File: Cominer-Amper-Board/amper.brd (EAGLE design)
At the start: 54.3 x 61 mm, 3 parts, among them U1 ESP-07

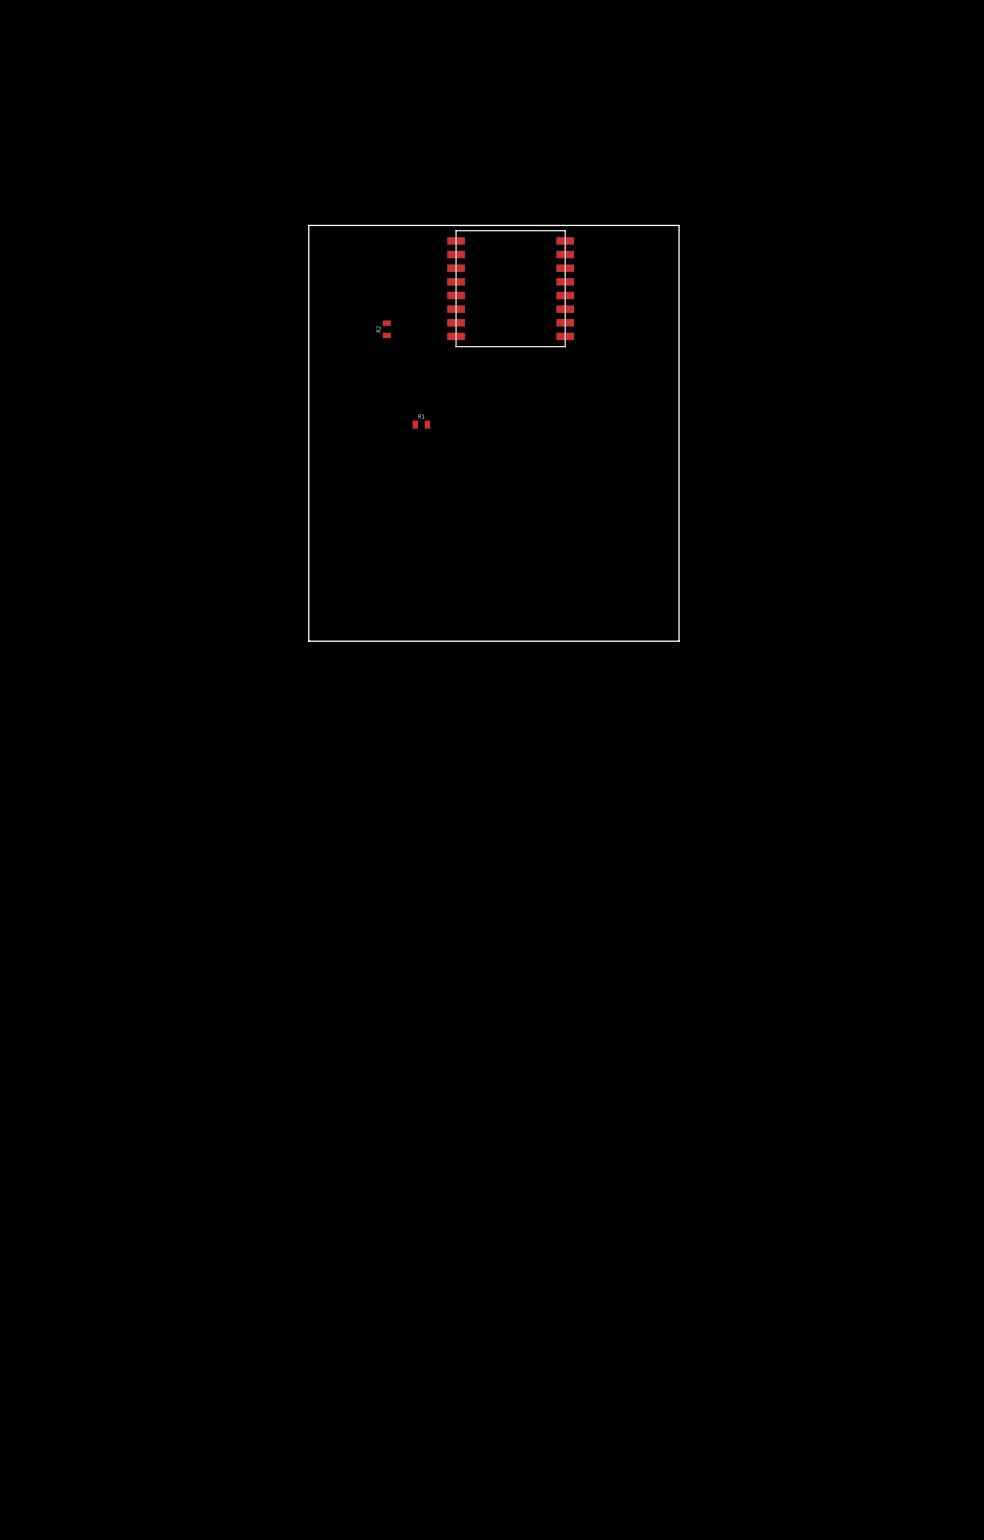
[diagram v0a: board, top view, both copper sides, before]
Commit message: add usb to serialport circuit and lm1117 regulator
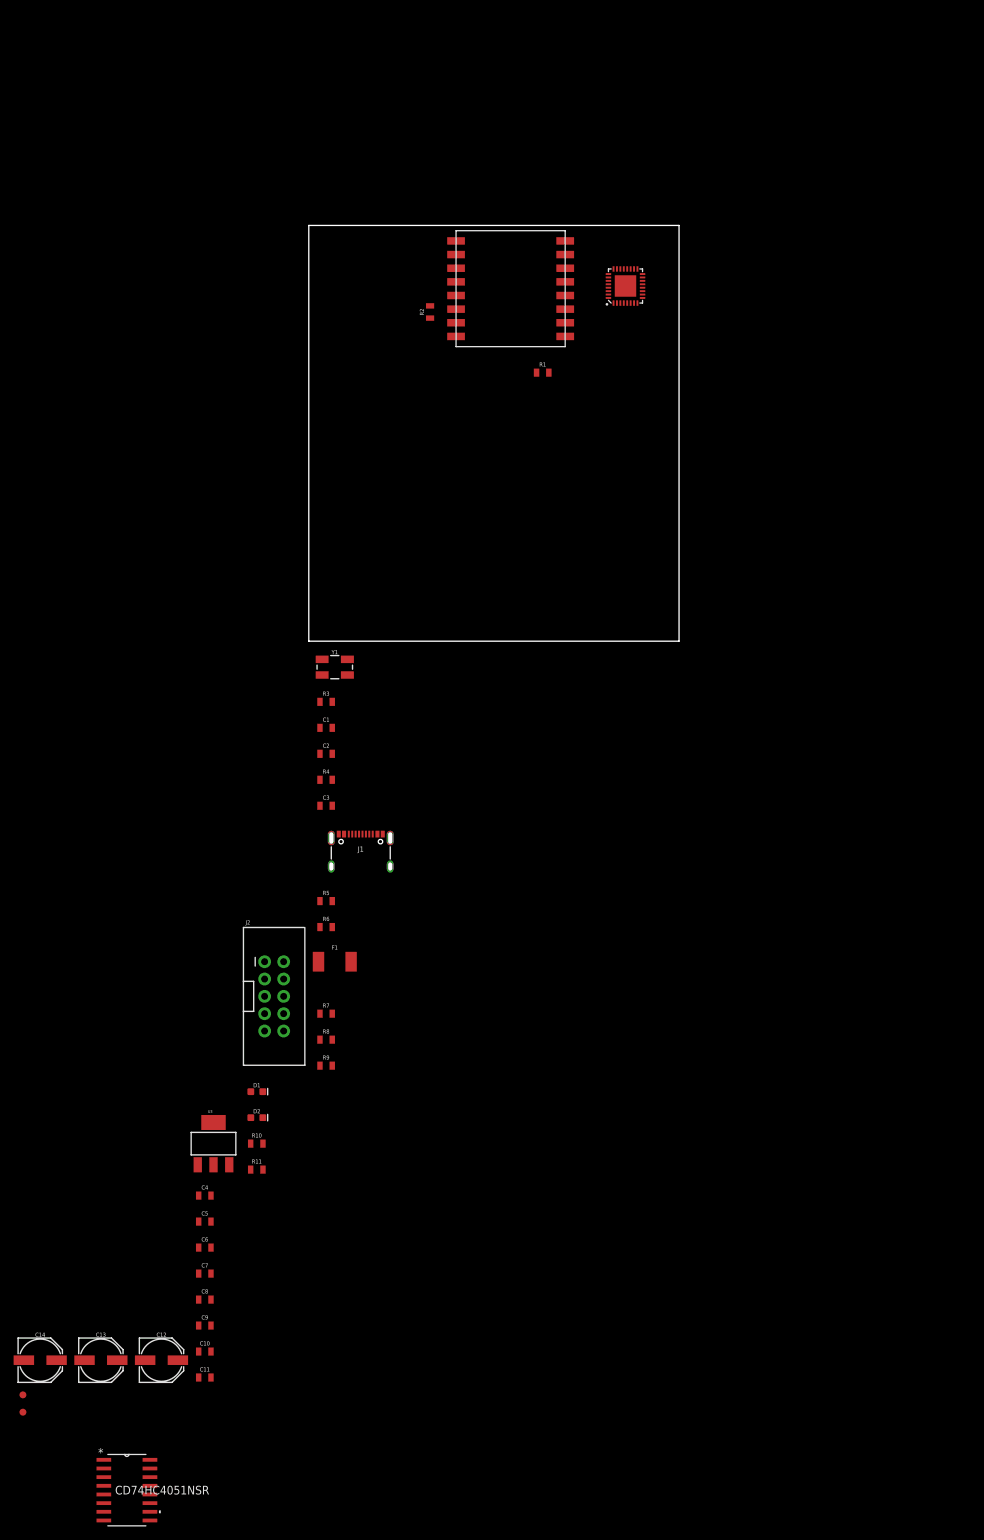
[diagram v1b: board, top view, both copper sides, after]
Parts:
- added C1, C2, C5, C6, C7, C8: 22p, SparkFun-Capacitors:0805
- added C10, C11, C3, C4, C9: 1u, SparkFun-Capacitors:0805
- added C12, C13, C14: 100uF, SparkFun-Capacitors:PANASONIC_D
- added D1, D2: Yellow, SparkFun-LED:LED-0603
- added F1: 500mA, SparkFun-Fuses:1812
- added J1: (no value), SparkFun-Connectors:USB-C-16P-2LAYER-PADS
- added J2: AVR_SPI_PROG_5X2LOCK, SparkFun-Connectors:2X5-SHROUDED_LOCK
- added R10, R11: 1k, SparkFun-Resistors:0805
- added R3: 10M, SparkFun-Resistors:0805
- added R4, R7, R8, R9: 10k, SparkFun-Resistors:0805
- added R5, R6: 22, SparkFun-Resistors:0805
- added TP2: 3.3v, SparkFun-Connectors:PAD.03X.04
- added TP3: 5v, SparkFun-Connectors:PAD.03X.04
- added U2: ATMEGA16U2, Cominer-Microcontroller:QFN32
- added U3: LM1117-3.3v, SparkFun-IC-Power:SOT223
- added U4: CD74HC4051NSR, Cominer-CD74HC4051NSR:NS16
- added Y1: 16MHz, SparkFun-Clocks:CRYSTAL-SMD-5X3.2-4PAD
- R1, R2: value (none) -> 10k
- moved R1 19.3 mm to (34.3, 39.4)
- moved R2 6.84 mm to (17.8, 48.3)
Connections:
- net ADC renamed ADC_ESP
- net RST renamed RST_ESP
- removed net RX: U1.RX0
- removed net TX: U1.TX0
- new net 5V: C10.2, C11.2, C12.+, C13.+, C14.+, C9.2, F1.2, J2.2, R10.2, R11.2, R4.1, R9.2, TP3.P$1, U2.31, U2.32, U2.4, U3.3
- new net MISO_AVR: J2.9, U2.17
- new net MOSI_AVR: J2.1, U2.16
- new net N$1: C1.2, R3.1, U2.1, Y1.3
- new net N$10: F1.1, J1.VBUS1, J1.VBUS2
- new net N$11: R7.1, U2.8
- new net N$12: D1.C, U2.11
- new net N$13: D2.A, R10.1
- new net N$15: D1.A, R11.1
- new net N$2: C2.2, R3.2, U2.2, Y1.1
- new net N$3: C3.2, U2.27
- new net N$4: D2.C, U2.10
- new net N$5: R8.1, U2.9
- new net N$6: R6.2, U2.30
- new net N$7: R5.2, R9.1, U2.29
- new net N$8: J1.A6, J1.B6, R5.1
- new net N$9: J1.A7, J1.B7, R6.1
- new net RST_AVR: J2.5, R4.2, U2.24
- new net RX_ESP: R8.2, U1.RX0
- new net SCK_AVR: J2.7, U2.15
- new net TX_ESP: R7.2, U1.TX0
- new net VCC: U4.16
- new net VEE: U4.7
- net 3.3V: now also C4.2, C5.2, C6.2, C7.2, C8.2, TP2.P$1, U3.2
- net GND: now also C1.1, C10.1, C11.1, C12.-, C13.-, C14.-, C2.1, C3.1, C4.1, C5.1, C6.1, C7.1, C8.1, C9.1, J1.GND, J1.GND2, J1.SHLD1, J1.SHLD2, J1.SHLD3, J1.SHLD4, J2.10, J2.4, J2.6, J2.8, U2.28, U2.3, U2.EP, U3.1, U4.8

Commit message: all devices were order
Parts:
- removed C10, C11, C9: 1u, SparkFun-Capacitors:0805
- removed C13, C14: 100uF, SparkFun-Capacitors:PANASONIC_D
- removed C7, C8: 22p, SparkFun-Capacitors:0805
- removed D1, D2: Yellow, SparkFun-LED:LED-0603
- removed R10, R11: 1k, SparkFun-Resistors:0805
- removed R7, R8: 10k, SparkFun-Resistors:0805
- removed TP2: 3.3v, SparkFun-Connectors:PAD.03X.04
- removed TP3: 5v, SparkFun-Connectors:PAD.03X.04
- added C17, C18, C19: 0.1u, SparkFun-Capacitors:0805
- added C20: 1u, SparkFun-Capacitors:0805
- added C23: 100uF, SparkFun-Capacitors:PANASONIC_D
- added D3: STATUS, SparkFun-LED:LED-0603
- added D4: ALARM, SparkFun-LED:LED-0603
- added D5: POWER, SparkFun-LED:LED-0603
- added IC1: OP-AMP, SparkFun-IC-Amplifiers:SO08
- added J3, J4, J5, J6: AUDIO_JACK_3.5MM_PTH, SparkFun-Connectors:AUDIO-JACK
- added J7: MOLEX-CPU-POWER, Cominer-Connectors:MOLEX-5.08-4PIN
- added J8: POWER_JACKSLT, SparkFun-Connectors:POWER_JACK_SLOT
- added Q1, Q2, Q3, Q4, Q5, Q6: 220mA/50V/3.5Ω, SparkFun-DiscreteSemi:SOT23-3
- added Q7: 20V/2A, SparkFun-DiscreteSemi:SOT23-3
- added R12, R13, R14, R15, R16, R17, R18, R19, R20, R21, R22, R23, R24, R25: 10k, SparkFun-Resistors:0805
- added R26, R27, R28: 1k, SparkFun-Resistors:0805
- added U5, U6: ADS1015, SparkFun-IC-Conversion:MSOP10
- C4: value 1u -> 0.1u
- C5, C6: value 22p -> 0.1u
- U4: value CD74HC4051NSR -> LM1117-5v; device Cominer-CD74HC4051NSR:NS16 -> SparkFun-IC-Power:SOT223
- moved U4 198.2 mm to (45.8, 60.0), turned to 180 degrees
- moved C12 189.3 mm to (45.7, 71.5), turned to 90 degrees
- moved C6 159.8 mm to (36.8, 62.2), turned to 270 degrees
- moved R9 155.4 mm to (66.2, 79.5), turned to 90 degrees
- moved C4 153.3 mm to (68.9, 46.8), turned to 90 degrees
- moved C5 152.2 mm to (68.9, 41.7), turned to 90 degrees
- moved J2 148.0 mm to (84.0, 66.1)
- moved F1 144.9 mm to (74.6, 79.4)
- moved U3 141.2 mm to (31.4, 60.0), turned to 180 degrees
- moved R6 138.8 mm to (69.9, 79.5), turned to 270 degrees
- moved R5 134.6 mm to (68.1, 79.5), turned to 270 degrees
- moved J1 127.8 mm to (71.4, 82.8), turned to 180 degrees
- moved C3 122.4 mm to (73.0, 76.0)
- moved R4 121.2 mm to (76.2, 76.0), turned to 180 degrees
- moved C1 107.1 mm to (63.8, 75.2), turned to 180 degrees
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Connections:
- removed net ADC_ESP: U1.ADC
- removed net N$11: R7.1, U2.8
- removed net N$12: D1.C, U2.11
- removed net N$13: D2.A, R10.1
- removed net N$15: D1.A, R11.1
- removed net N$4: D2.C, U2.10
- removed net N$5: R8.1, U2.9
- removed net VCC: U4.16
- removed net VEE: U4.7
- new net N$16: J3.SLEEVE, U5.4
- new net N$17: J3.TIP, U5.5
- new net N$18: J4.TIP, U5.7
- new net N$19: J4.SLEEVE, U5.6
- new net N$20: J5.TIP, U6.5
- new net N$21: Q1.3, R14.2, U5.9
- new net N$22: J5.SLEEVE, U6.4
- new net N$23: Q2.3, R13.2, U5.10
- new net N$24: J6.TIP, U6.7
- new net N$25: J6.SLEEVE, U6.6
- new net N$26: Q3.3, R17.2, U6.10
- new net N$27: Q4.3, R18.2, U6.9
- new net N$28: IC1.1, Q7.1
- new net N$29: IC1.3, R24.1, R25.2
- new net N$30: D3.C, U1.I016
- new net N$31: D4.C, U1.IO14
- new net N$32: D3.A, R26.2
- new net N$33: D4.A, R27.2
- new net N$36: D5.A, R28.1
- new net RX_AVR: Q6.3, R22.2, U2.8
- new net SCL_ADC: Q2.2, Q3.2, R12.2, R16.2, U1.IO5
- new net SDA_ADC: Q1.2, Q4.2, R15.2, R19.2, U1.IO4
- new net TX_AVR: Q5.3, R21.2, U2.9
- new net USBVCC: F1.2, Q7.3, R9.2, U2.31
- new net VIN: C12.+, C20.2, C23.+, J7.12VCD, J8.PWR, R24.2, U4.3
- net 3.3V: now also IC1.2, Q1.1, Q2.1, Q3.1, Q4.1, Q5.1, Q6.1, R12.1, R15.1, R16.1, R19.1, R20.1, R23.1; no longer C7.2, C8.2, TP2.P$1
- net 5V: now also C17.2, C18.2, C19.2, IC1.8, J3.TSH, J4.TSH, J5.TSH, J6.TSH, Q7.2, R13.1, R14.1, R17.1, R18.1, R21.1, R22.1, R26.1, R27.1, R28.2, U4.2, U5.1, U5.8, U6.8; no longer C10.2, C11.2, C12.+, C13.+, C14.+, C9.2, F1.2, R10.2, R11.2, R9.2, TP3.P$1, U2.31
- net GND: now also C17.1, C18.1, C19.1, C20.1, C23.-, D5.C, IC1.4, J7.GND, J7.GND2, J8.GND@1, J8.GND@2, R25.1, U4.1, U5.3, U6.1, U6.3; no longer C10.1, C11.1, C13.-, C14.-, C7.1, C8.1, C9.1, U4.8
- net N$1: now also Y1.1; no longer Y1.3
- net N$2: now also Y1.3; no longer Y1.1
- net RX_ESP: now also Q5.2, R20.2; no longer R8.2
- net TX_ESP: now also Q6.2, R23.2; no longer R7.2
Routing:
- net GND: track 0.00 -> 187.1 mm
- net 3.3V: track 0.00 -> 102.4 mm, vias 0 -> 2
- net 5V: track 0.00 -> 82.5 mm, vias 0 -> 2
- net RX_AVR: track 0.00 -> 76.6 mm, vias 0 -> 2
- net SDA_ADC: track 0.00 -> 75.0 mm
- net SCL_ADC: track 0.00 -> 71.0 mm, vias 0 -> 2
- net TX_AVR: track 0.00 -> 60.4 mm, vias 0 -> 2
- net N$30: track 0.00 -> 49.6 mm, vias 0 -> 2
- net N$31: track 0.00 -> 48.1 mm, vias 0 -> 2
- net VIN: track 0.00 -> 39.8 mm
- net N$20: track 0.00 -> 32.4 mm
- net N$17: track 0.00 -> 31.2 mm
- net RST_AVR: track 0.00 -> 21.1 mm
- net N$25: track 0.00 -> 20.4 mm
- net N$19: track 0.00 -> 19.6 mm
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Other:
- board size 54.3 x 61 mm -> 95 x 90 mm

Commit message: cominer-amp board complete
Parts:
- added C10, C11, C13, C7, C8, C9: 0.1u, SparkFun-Capacitors:0805
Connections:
- net 5V: now also C10.2, C11.2, C13.2, C7.2, C8.2, C9.2
- net GND: now also C10.1, C11.1, C13.1, C7.1, C8.1, C9.1
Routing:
- net 5V: track 82.5 -> 323.8 mm, vias 2 -> 11
- net GND: track 187.1 -> 354.7 mm, vias 0 -> 24
- net 3.3V: track 102.4 -> 208.9 mm, vias 2 -> 7
- net USBVCC: track 11.6 -> 98.0 mm, vias 0 -> 3
- net VIN: track 39.8 -> 77.9 mm, vias 0 -> 1
- net N$10: track 12.3 -> 14.2 mm, vias 0 -> 2
- added copper zone on layer 1, net GND
- added copper zone on layer 16, net GND
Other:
- outline, holes or cut-outs redrawn
- board text added: "AMPER"
- board text added: "COMINER"
- board text added: "MINER PUNK"
- board text added: "U2"
- board text added: "v1.0"

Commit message: amper board is ready
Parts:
- moved U5 1.50 mm to (63.6, 16.9)
- moved C1 1.50 mm to (63.8, 73.7)
- moved C10 1.50 mm to (52.3, 15.4)
- moved C11 1.50 mm to (83.8, 76.6)
- moved C12 1.50 mm to (45.7, 70.0)
- moved C13 1.50 mm to (69.8, 18.1)
- moved C17 1.50 mm to (66.8, 64.1)
- moved C18 1.50 mm to (31.2, 19.9)
- moved C19 1.50 mm to (63.6, 19.6)
- moved C2 1.50 mm to (60.8, 68.1)
- moved C20 1.50 mm to (38.6, 68.5)
- moved C23 1.50 mm to (31.4, 70.0)
- moved C3 1.50 mm to (73.0, 74.5)
- moved C6 1.50 mm to (36.8, 60.7)
- moved C7 1.50 mm to (66.8, 61.6)
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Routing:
- net GND: track 354.7 -> 364.1 mm, vias 24 -> 29
- net 3.3V: track 208.9 -> 203.3 mm
- net VIN: track 77.9 -> 80.6 mm
- net RX_AVR: track 76.6 -> 74.9 mm
- net TX_ESP: track 9.15 -> 7.65 mm
- net N$31: track 48.1 -> 46.6 mm
- net N$30: track 49.6 -> 48.1 mm
- net RX_ESP: track 10.2 -> 8.96 mm
- net TX_AVR: track 60.4 -> 59.3 mm
- net N$26: track 15.8 -> 16.8 mm
- net SCL_ADC: track 71.0 -> 70.1 mm
- net 5V: track 323.8 -> 323.1 mm
- net N$25: track 20.4 -> 19.8 mm
- net N$27: track 16.5 -> 17.1 mm
- net N$2: track 13.5 -> 14.0 mm
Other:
- board size 95 x 90 mm -> 92 x 87 mm
